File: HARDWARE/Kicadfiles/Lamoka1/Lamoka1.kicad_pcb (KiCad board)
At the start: 2 copper layers, 156.4 x 124.8 mm, 139 parts, among them IC1 INA240A2DR, J1 2606-1108/010-000, J2 2606-1352, J3 USB_C_Receptacle_USB2.0_14P, J4 470531000, J5 2604-1103, J6 Male-Header, J7 Male-Header, Q1 25V 60A N-Ch, Q2 30V 56A N-Ch, Q3 100V 150A N-Ch, Q4 100V 150A N-Ch, Q5 100V 150A N-Ch, Q6 100V 150A N-Ch, SW1 B3F-4055, U1 RP2354A, U10 ADS7128IRTER, U2 AMS1117-3.3, U3 74AHCT1G125, U4 LM5122MH/NOPB, U5 UCC27735DR, U6 UCC27735DR, U7 TPS62160DSGR, U8 TMP235A2DBZR, U9 TMP235A2DBZR, X1 ABM8-272-T3

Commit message: misc fixes
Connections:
- net /Battery-Connection  renamed +BATT
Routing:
- net GND: track 29.3 -> 31.6 mm
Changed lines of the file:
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@@
 		(sheetname "/Inversion-Section/")
 		(sheetfile "Inversion-section.kicad_sch")
+		(units
+			(unit
+				(name "A")
+				(pins "2" "1" "3")
+			)
+		)
 		(attr smd)
 		(duplicate_pad_numbers_are_jumpers no)
@@
 		(sheetname "/")
 		(sheetfile "Lamoka1.kicad_sch")
+		(units
+			(unit
+				(name "A")
+				(pins "1" "2" "3" "4" "5" "6")
+			)
+		)
 		(attr through_hole)
 		(duplicate_pad_numbers_are_jumpers no)
@@
 			(layers "F.Cu" "F.Mask" "F.Paste")
 			(roundrect_rratio 0.204082)
-			(net "/Battery-Connection ")
+			(net "+BATT")
 			(pintype "passive")
 		)
@@
 			(net "unconnected-(U10-AIN5{slash}GPIO5-Pad4)")
 			(pinfunction "AIN5/GPIO5_4")
-			(pintype "bidirectional")
+			(pintype "bidirectional+no_connect")
 		)
 		(pad "5" smd rect
@@
 			(net "unconnected-(U10-AIN6{slash}GPIO6-Pad5)")
 			(pinfunction "AIN6/GPIO6_5")
-			(pintype "bidirectional")
+			(pintype "bidirectional+no_connect")
 		)
 		(pad "6" smd rect
@@
 			(net "unconnected-(U10-AIN7{slash}GPIO7-Pad6)")
 			(pinfunction "AIN7/GPIO7_6")
-			(pintype "bidirectional")
+			(pintype "bidirectional+no_connect")
 		)
 		(pad "7" smd rect
@@
 			(net "GND")
 			(pinfunction "GND_9")
-			(pintype "power_out")
+			(pintype "power_in")
 		)
 		(pad "10" smd rect
@@
 			(net "GND")
 			(pinfunction "GND_17")
-			(pintype "power_out")
+			(pintype "power_in")
 		)
 		(embedded_fonts no)
@@
 			(net "/Control-Section/PG")
 			(pinfunction "PG_8")
-			(pintype "input")
+			(pintype "open_collector")
 		)
 		(pad "9" smd rect
@@
 			(net "GND")
 			(pinfunction "VSS_3")
-			(pintype "power_out")
+			(pintype "power_in")
 		)
 		(pad "4" smd rect
@@
 			(net "GND")
 			(pinfunction "COM_5")
-			(pintype "output")
+			(pintype "passive")
 		)
 		(pad "6" smd rect
@@
 		(sheetname "/Inversion-Section/")
 		(sheetfile "Inversion-section.kicad_sch")
+		(units
+			(unit
+				(name "A")
+				(pins "2" "1" "3")
+			)
+		)
 		(attr smd)
 		(duplicate_pad_numbers_are_jumpers no)
@@
 			(net "unconnected-(U4-SYNCOUT-Pad1)")
 			(pinfunction "SYNCOUT_1")
-			(pintype "output")
+			(pintype "output+no_connect")
 		)
 		(pad "2" smd rect
@@
 		(sheetname "/Control-Section/")
 		(sheetfile "Control-section.kicad_sch")
+		(units
+			(unit
+				(name "A")
+				(pins "1" "2")
+			)
+		)
 		(attr smd)
 		(duplicate_pad_numbers_are_jumpers no)
@@
 			(net "GND")
 			(pinfunction "VSS_3")
-			(pintype "power_out")
+			(pintype "power_in")
 		)
 		(pad "4" smd rect
@@
 			(net "GND")
 			(pinfunction "COM_5")
-			(pintype "output")
+			(pintype "passive")
 		)
 		(pad "6" smd rect
@@
 		(sheetname "/")
 		(sheetfile "Lamoka1.kicad_sch")
+		(units
+			(unit
+				(name "A")
+				(pins "1" "2" "3" "4" "5" "6" "7" "8")
+			)
+		)
 		(attr through_hole)
 		(duplicate_pad_numbers_are_jumpers no)
@@
 			(size 0.65 1.528)
 			(layers "F.Cu" "F.Mask" "F.Paste")
-			(net "/Battery-Connection ")
+			(net "+BATT")
 			(pinfunction "IN+_8")
 			(pintype "passive")
@@
 		(sheetname "/Control-Section/")
 		(sheetfile "Control-section.kicad_sch")
+		(units
+			(unit
+				(name "A")
+				(pins "1" "2")
+			)
+		)
 		(attr smd)
 		(duplicate_pad_numbers_are_jumpers no)
@@
 		(sheetname "/Control-Section/")
 		(sheetfile "Control-section.kicad_sch")
+		(units
+			(unit
+				(name "A")
+				(pins "1" "2")
+			)
+		)
 		(attr smd)
 		(duplicate_pad_numbers_are_jumpers no)
@@
 			(layers "*.Cu" "*.Mask")
 			(remove_unused_layers no)
-			(net "/Battery-Connection ")
+			(net "+BATT")
 			(pinfunction "1_1_1")
 			(pintype "unspecified")
@@
 			(layers "*.Cu" "*.Mask")
 			(remove_unused_layers no)
-			(net "/Battery-Connection ")
+			(net "+BATT")
 			(pinfunction "1_2_2")
 			(pintype "unspecified")
@@
 			(net "/Control-Section/3v3")
 			(pinfunction "VOUT_2")
-			(pintype "output")
+			(pintype "power_out")
 		)
 		(pad "2" smd roundrect
@@
 			(net "/Control-Section/3v3")
 			(pinfunction "VOUT_2")
-			(pintype "output")
+			(pintype "power_out")
 		)
 		(pad "3" smd roundrect
@@
 	)
 	(segment
+		(start 140.185558 117.576297)
+		(end 139.86056 117.251299)
+		(width 0.4)
+		(layer "F.Cu")
+		(net "GND")
+	)
+	(segment
 		(start 111.518109 95.568109)
 		(end 111.518109 95.524454)
@@
 	)
 	(segment
+		(start 140.185558 119.426301)
+		(end 140.185558 117.576297)
+		(width 0.4)
+		(layer "F.Cu")
+		(net "GND")
+	)
+	(segment
 		(start 109.663201 102.2068)
 		(end 109.663201 102.929999)
@@
 	)
 	(via
-		(at 88.55 134.77)
+		(at 88.77 135.4)
 		(size 0.6)
 		(drill 0.3)
@@
 	)
 	(via
-		(at 140.185558 118.775)
+		(at 137.67 114.46)
 		(size 0.6)
 		(drill 0.3)
@@
 	)
 	(via
-		(at 88.48 136.04)
+		(at 88.79 138.1)
 		(size 0.6)
 		(drill 0.3)
@@
 	)
 	(segment
-		(start 102.761 133.2835)
-		(end 99.7575 130.28)
-		(width 0.55)
-		(layer "F.Cu")
-		(net "/Battery-Connection ")
-	)
-	(segment
-		(start 65.2 129.97)
-		(end 65.2 142.47)
-		(width 2.25)
-		(layer "F.Cu")
-		(net "/Battery-Connection ")
-	)
-	(segment
-		(start 102.761 135.485)
-		(end 102.761 133.2835)
-		(width 0.55)
-		(layer "F.Cu")
-		(net "/Battery-Connection ")
-	)
-	(segment
 		(start 113.38 115.05)
 		(end 110.300733 118.129267)
@@
 		(net "/Inversion-Section/HB1")
 	)
+	(segment
+		(start 102.761 133.2835)
+		(end 99.7575 130.28)
+		(width 0.55)
+		(layer "F.Cu")
+		(net "+BATT")
+	)
+	(segment
+		(start 65.2 129.97)
+		(end 65.2 142.47)
+		(width 2.25)
+		(layer "F.Cu")
+		(net "+BATT")
+	)
+	(segment
+		(start 102.761 135.485)
+		(end 102.761 133.2835)
+		(width 0.55)
+		(layer "F.Cu")
+		(net "+BATT")
+	)
 	(zone
 		(net "/BROWN")
@@
 	)
 	(zone
-		(net "/Battery-Connection ")
-		(layer "F.Cu")
-		(name "Battery-connection")
-		(hatch edge 0.5)
-		(priority 46)
-		(connect_pads yes
-			(clearance 0.25)
-		)
-		(min_thickness 0.1)
-		(fill yes
-			(thermal_gap 0.5)
-			(thermal_bridge_width 0.5)
-			(smoothing fillet)
-			(radius 0.55)
-			(island_removal_mode 0)
-		)
-		(polygon
-			(pts
-				(xy 100.41 128.54) (xy 100.44 131.93) (xy 95.44 131.8) (xy 91.73 132.31) (xy 90.64 132.8) (xy 89.22 133.15)
-				(xy 88.24 133.66) (xy 87.27 134.55) (xy 86.84 136.11) (xy 85.93 137.07) (xy 83.86 138.29) (xy 81.76 138.97)
-				(xy 80.37 139.35) (xy 78.62 139.27) (xy 76.05 139.68) (xy 71.44 141.15) (xy 69.5 141.98) (xy 68.1 142.94)
-				(xy 65.93 144.56) (xy 63.48 145.04) (xy 62.84 144.31) (xy 62.41 141.9) (xy 62.29 140.01) (xy 62.57 137.2)
-				(xy 62.44 134.9) (xy 62.36 132.93) (xy 62.77 131.49) (xy 62.97 130.28) (xy 63.12 128.63) (xy 64.01 128.1)
-				(xy 64.61 127.97) (xy 65.98 128.02) (xy 67.12 128.45) (xy 67.7 129.41) (xy 68.13 130.28) (xy 74.22 131.41)
-				(xy 75.36 132.67) (xy 76.98 133.36) (xy 79.33 132.95) (xy 80.83 132.32) (xy 82.52 130.28) (xy 83.78 128.75)
-			)
-		)
-	)
-	(zone
 		(net "Net-(U1-VREG_AVDD)")
 		(layer "F.Cu")
@@
 	)
 	(zone
+		(net "+BATT")
+		(layer "F.Cu")
+		(name "batt")
+		(hatch edge 0.5)
+		(priority 46)
+		(connect_pads yes
+			(clearance 0.5)
+		)
+		(min_thickness 0.25)
+		(fill yes
+			(thermal_gap 0.5)
+			(thermal_bridge_width 0.5)
+			(smoothing fillet)
+			(radius 0.5)
+			(island_removal_mode 0)
+		)
+		(polygon
+			(pts
+				(xy 63.38121 128.16751) (xy 63.238811 144.35) (xy 67.51 144.39) (xy 71.81 139.44) (xy 73.51 137.49)
+				(xy 93.679075 132.103717) (xy 100.534871 132.156699) (xy 100.56 128.460928) (xy 98.55631 128.449265)
+				(xy 94 128.51) (xy 73.13 133.21) (xy 66.755645 128.086308)
+			)
+		)
+	)
+	(zone
 		(net "/Inversion-Section/Q4G")
 		(layer "F.Cu")
@@
 		(name "GND")
 		(hatch edge 0.5)
-		(connect_pads
+		(connect_pads yes
 			(clearance 0.5)
 		)

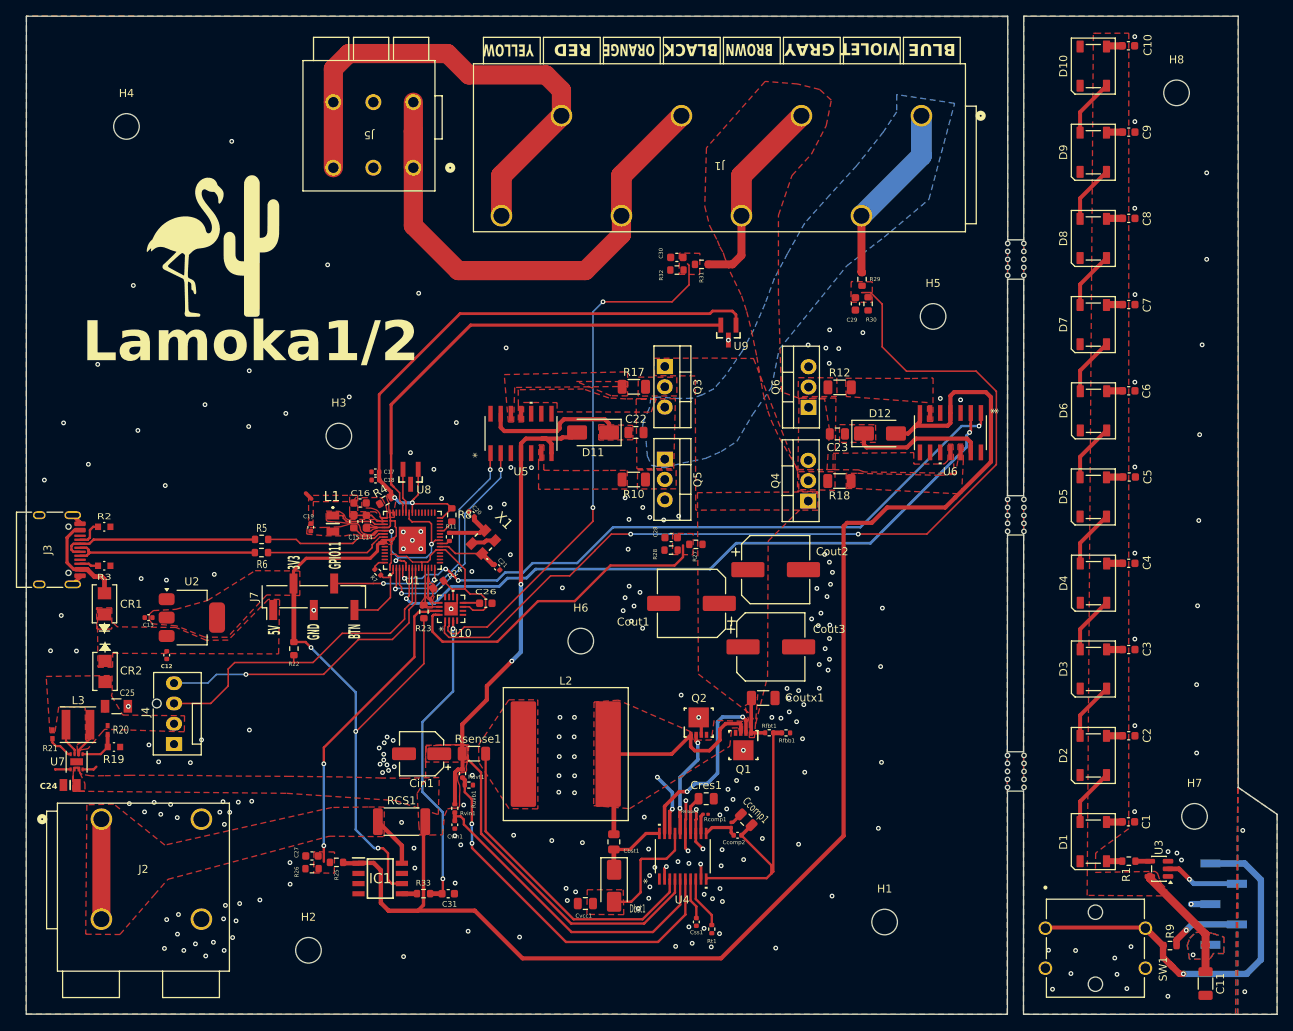
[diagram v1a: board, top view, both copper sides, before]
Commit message: General fixes, laying H bridge transformers side by side for more effective heat dissapation. fixed footprints to datasheet specific
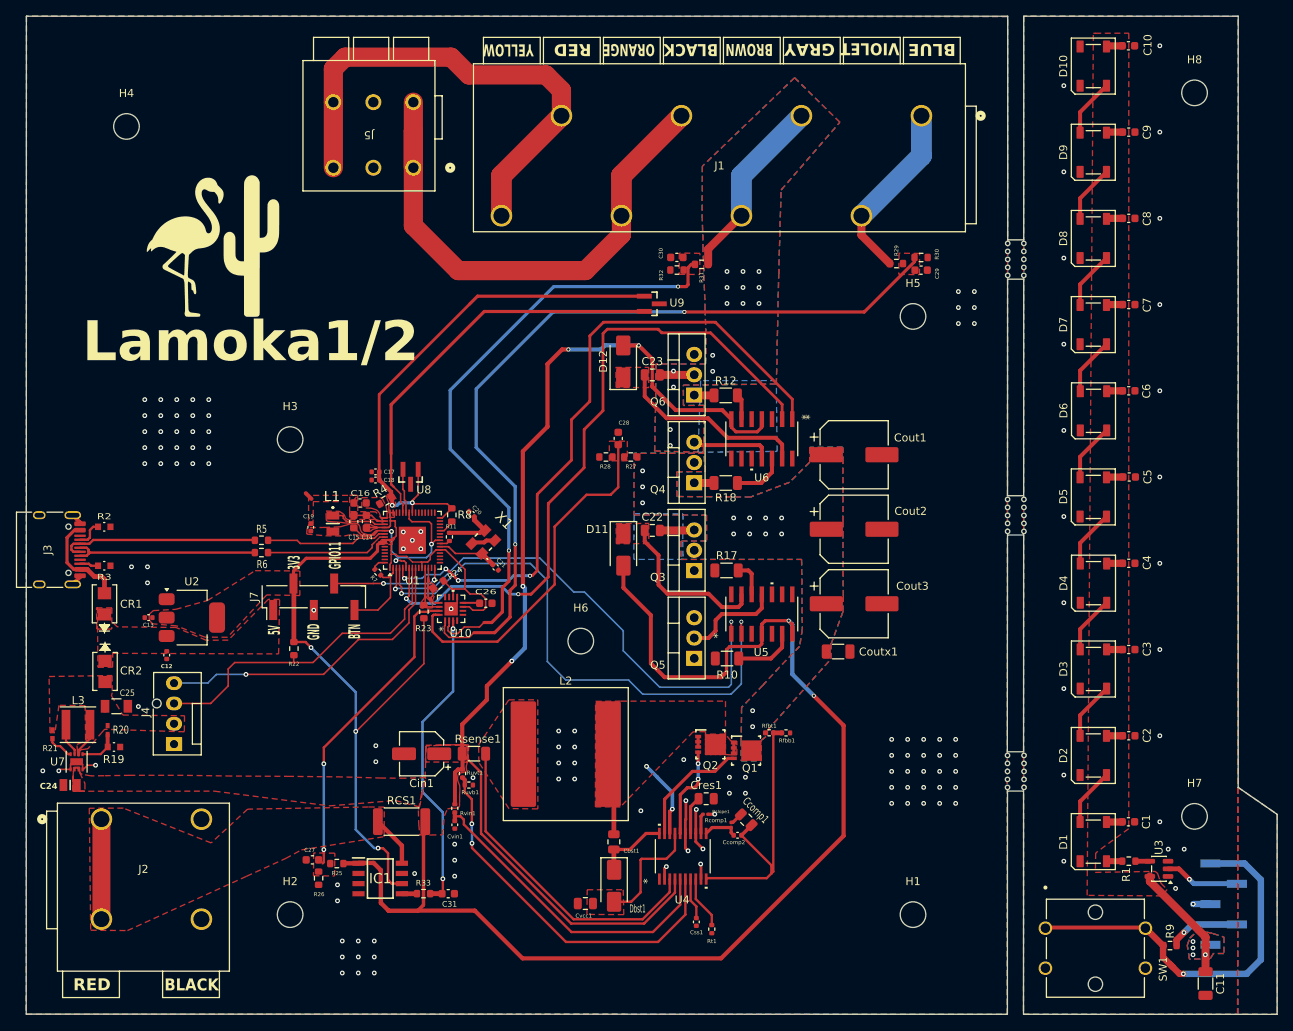
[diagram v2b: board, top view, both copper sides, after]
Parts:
- moved U5 37.6 mm to (147.8, 104.3)
- moved D12 33.3 mm to (130.4, 72.8), turned to 90 degrees
- moved Cout1 27.5 mm to (159.3, 84.4), turned to 0 degrees
- moved Q3 25.8 mm to (139.3, 98.9), turned to 90 degrees
- moved R17 25.7 mm to (143.3, 98.9), turned to 180 degrees
- moved R10 25.2 mm to (143.4, 109.9), turned to 0 degrees
- moved Q5 25.2 mm to (139.3, 109.9), turned to 90 degrees
- moved C23 24.3 mm to (134.1, 74.4), turned to 0 degrees
- moved U6 23.6 mm to (147.8, 82.4)
- moved D11 15.1 mm to (130.4, 96.3), turned to -90 degrees
- moved Q4 14.4 mm to (139.3, 87.9)
- moved Q6 14.4 mm to (139.3, 77.0)
- moved R12 14.3 mm to (143.2, 77.0)
- moved R18 14.2 mm to (143.2, 88.0)
- moved R28 14.2 mm to (128.3, 84.7)
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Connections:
- Q1 pad 1: /Inversion-Section/G4D -> /Inversion-Section/SW
- Q1 pad 2: /Inversion-Section/HO -> /Inversion-Section/SW
- Q1 pad 4: (no net) -> /Inversion-Section/HO
- Q1 pad 9: GND -> /Inversion-Section/G4D
- Q2 pad 1: /Inversion-Section/SW -> GND
- Q2 pad 2: /Inversion-Section/LO -> GND
- Q2 pad 4: (no net) -> /Inversion-Section/LO
- Q2 pad 9: GND -> /Inversion-Section/SW
- Q3 pad 1: /Inversion-Section/G4D -> /Inversion-Section/Q3G
- Q3 pad 2: /Inversion-Section/Q3G -> /Inversion-Section/G4D
- Q4 pad 1: /Inversion-Section/G4D -> /Inversion-Section/Q4G
- Q4 pad 2: /Inversion-Section/Q4G -> /Inversion-Section/G4D
- Q5 pad 1: /BLUE -> /Inversion-Section/Q5G
- Q5 pad 2: /Inversion-Section/Q5G -> /BLUE
- Q6 pad 1: /BROWN -> /Inversion-Section/Q6G
- Q6 pad 2: /Inversion-Section/Q6G -> /BROWN
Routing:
- net /Control-Section/GPIO2: track 28.4 -> 70.0 mm
- net /Control-Section/GPIO1: track 27.4 -> 64.1 mm
- net /Inversion-Section/CSP: track 277.5 -> 299.3 mm, vias 2 -> 6
- net /Inversion-Section/SW: track 40.8 -> 21.5 mm
- net /BLUE: track 22.7 -> 39.9 mm
- net /BROWN: track 25.2 -> 37.8 mm, vias 0 -> 15
- net /Control-Section/3v3: track 197.6 -> 186.2 mm
- net /Control-Section/AIN3: track 67.7 -> 78.8 mm
- net /Control-Section/AIN2: track 114.0 -> 103.8 mm
- net /Control-Section/TEMP_INV: track 59.4 -> 50.6 mm
- net /Inversion-Section/HO: track 23.7 -> 15.0 mm, vias 2 -> 0
- net /Inversion-Section/LO1: track 0.00 -> 7.70 mm
- net /Inversion-Section/HB2: track 16.8 -> 24.1 mm
- net Net-(U6-HO): track 0.00 -> 6.59 mm
- net /Inversion-Section/G4D: track 6.11 -> 0.00 mm, vias 0 -> 11
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- added copper zone on B.Cu, net /BROWN
- added copper zone on B.Cu, net /Inversion-Section/G4D
- removed copper zone on B.Cu, net /BLUE
- removed copper zone on F.Cu, net /BLUE
- removed copper zone on F.Cu, net /Inversion-Section/LO1
- removed copper zone on F.Cu, net /Inversion-Section/LO2
- removed copper zone on F.Cu, net /Inversion-Section/Q3G
- removed copper zone on F.Cu, net /Inversion-Section/Q4G
- removed copper zone on F.Cu, net /Inversion-Section/Q5G
- removed copper zone on F.Cu, net /Inversion-Section/Q6G
- removed copper zone on F.Cu, net Net-(U5-HO)
- removed copper zone on F.Cu, net Net-(U6-HO)

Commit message: major reform on the size of the Lamoka1/2
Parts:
- removed C10, C6, C7, C8, C9: 100n, Capacitor_SMD:C_0603_1608Metric
- removed D10, D7, D8, D9: WS2812B, LED_SMD:LED_WS2812B_PLCC4_5.0x5.0mm_P3.2mm
- removed the D6 at (189.2, 78.9)
- removed J6, J7: Male-Header, Connector_PinHeader_2.54mm:PinHeader_1x05_P2.54mm_Vertical_SMD_Pin1Left
- removed MTB1, MTB2, MTB3: MouseBite-5x0.55, MouseBite-5x0.55
- C12, C13, C20, C21, C24, C25, CR1, CR2, D11, D12, J3, L1, R11, R19, R2, R20, R21, R3, R5, R6, R8, U1, U10, U2, U5, U6, U7, X1: moved to B.Cu
- L3: value 2.2uH, 4.3A -> 2.2uH; moved to B.Cu
- moved G*** 455.0 mm to (517.3, 181.2)
- moved C13 387.0 mm to (395.9, 315.3)
- moved U2 387.0 mm to (401.3, 315.3)
- moved C12 382.0 mm to (398.1, 310.6), turned to -90 degrees
- moved CR1 378.0 mm to (380.4, 312.3)
- moved CR2 341.3 mm to (349.7, 300.7)
- moved L3 334.8 mm to (349.9, 289.4), turned to -90 degrees
- moved R21 332.9 mm to (346.2, 287.8), turned to 180 degrees
- moved U7 330.0 mm to (344.9, 292.8), turned to 0 degrees
- moved R20 327.9 mm to (346.2, 289.1), turned to 180 degrees
- moved D12 327.7 mm to (421.0, 224.2)
- moved C24 327.6 mm to (342.5, 293.8), turned to -90 degrees
- moved C25 327.4 mm to (347.0, 285.8), turned to 0 degrees
- moved D11 327.3 mm to (421.1, 246.8)
- moved R19 323.8 mm to (343.4, 289.1), turned to 180 degrees
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- renumbered Cbst1 to C32, Cvcc1 to C33, Dbst1 to D6
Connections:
- C1 pad 1: /User-Interface-Section/5V -> /Control-Section/5V
- C11 pad 1: /User-Interface-Section/5V -> /Control-Section/5V
- C2 pad 1: /User-Interface-Section/5V -> /Control-Section/5V
- C3 pad 1: /User-Interface-Section/5V -> /Control-Section/5V
- C4 pad 1: /User-Interface-Section/5V -> /Control-Section/5V
- C5 pad 1: /User-Interface-Section/5V -> /Control-Section/5V
- D1 pad 1: /User-Interface-Section/5V -> /Control-Section/5V
- D2 pad 1: /User-Interface-Section/5V -> /Control-Section/5V
- D3 pad 1: /User-Interface-Section/5V -> /Control-Section/5V
- D4 pad 1: /User-Interface-Section/5V -> /Control-Section/5V
- D5 pad 1: /User-Interface-Section/5V -> /Control-Section/5V
- D5 pad 2: Net-(D5-DOUT) -> unconnected-(D5-DOUT-Pad2)
- R9 pad 1: /User-Interface-Section/3v3 -> /Control-Section/3v3
- R9 pad 2: /User-Interface-Section/BTN -> /Control-Section/BTN
- SW1 pad 1: /User-Interface-Section/BTN -> /Control-Section/BTN
- SW1 pad 2: /User-Interface-Section/BTN -> /Control-Section/BTN
- U3 pad 2: /User-Interface-Section/GPIO11 -> /Control-Section/GPIO11
- U3 pad 5: /User-Interface-Section/5V -> /Control-Section/5V
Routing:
- net /Inversion-Section/G4D: track 0.00 -> 238.8 mm, vias 11 -> 0
- net /Inversion-Section/CSP: track 299.3 -> 82.5 mm, vias 6 -> 0
- net /Control-Section/3v3: track 186.2 -> 0.00 mm, vias 5 -> 0
- net /Control-Section/AIN2: track 103.8 -> 0.53 mm, vias 2 -> 0
- net /Control-Section/GPIO4: track 85.7 -> 0.00 mm, vias 2 -> 0
- net /Control-Section/GPIO3: track 84.2 -> 0.00 mm, vias 4 -> 0
- net /Control-Section/AIN3: track 78.8 -> 0.45 mm, vias 2 -> 0
- net /Control-Section/GPIO2: track 70.0 -> 0.00 mm, vias 2 -> 0
- net /Control-Section/GPIO1: track 64.1 -> 0.00 mm, vias 2 -> 0
- net /Control-Section/TEMP_INV: track 50.6 -> 0.00 mm
- net /User-Interface-Section/BTN: track 48.7 -> 0.00 mm, vias 1 -> 0
- net /Inversion-Section/UVLO: track 46.7 -> 1.00 mm, vias 2 -> 0
- net /Control-Section/AIN1: track 44.2 -> 0.00 mm
- net /GPIO5: track 42.2 -> 0.03 mm
- net /Inversion-Section/CSN: track 40.3 -> 0.00 mm
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- removed copper zone on F.Cu, net +BATT
- removed copper zone on B.Cu, net /BROWN
- removed copper zone on F.Cu, net /BROWN
- removed copper zone on F.Cu, net /Buck-5v
- removed copper zone on F.Cu, net /Control-Section/1V1
- removed copper zone on F.Cu, net /Control-Section/3v3
- removed copper zone on F.Cu, net /Control-Section/5V
- removed copper zone on F.Cu, net /Control-Section/AIN0
- removed copper zone on F.Cu, net /Control-Section/AIN1
- removed copper zone on F.Cu, net /Control-Section/GPIO8
- removed copper zone on F.Cu, net /Control-Section/GPIO9
- removed copper zone on F.Cu, net /Control-Section/VREG_GND
- removed copper zone on F.Cu, net /Inversion-Section/CSN
- removed copper zone on F.Cu, net /Inversion-Section/CSP
- removed copper zone on B.Cu, net /Inversion-Section/G4D
- removed copper zone on F.Cu, net /Inversion-Section/G4D
- removed copper zone on F.Cu, net /Inversion-Section/HB1
- removed copper zone on F.Cu, net /Inversion-Section/HB2
- removed copper zone on F.Cu, net /Inversion-Section/SW
- removed copper zone on F.Cu, net /Inversion-Section/VCC
- removed copper zone on B.Cu, net /User-Interface-Section/5V
- removed copper zone on F.Cu, net /User-Interface-Section/5V
- removed copper zone on B.Cu, net GND
- removed copper zone on F.Cu, net GND
- removed copper zone on F.Cu, net Net-(U1-VREG_AVDD)
- removed copper zone on F.Cu, net Net-(U1-VREG_LX)
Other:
- board size 156.4 x 124.8 mm -> 95 x 95 mm
- board text added: "Danger! High Voltage"
- board text removed: "3V3"
- board text removed: "5V"
- board text removed: "BTN"
- board text removed: "Danger! High Voltage."
- board text removed: "GND"
- board text removed: "GPIO11"

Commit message: misc fixes to the Lamoka1/2, more routing and all that fun stuff
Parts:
- moved H2 167.6 mm to (231.3, 128.7)
- moved R33 157.2 mm to (359.9, 249.6)
- moved C31 149.8 mm to (363.0, 249.6)
- moved H1 123.1 mm to (260.3, 164.2)
- moved H6 113.4 mm to (275.8, 152.4)
- moved H4 110.8 mm to (252.8, 118.8)
- moved H3 104.9 mm to (251.7, 145.1)
- moved CR1 94.6 mm to (342.2, 225.8)
- moved H5 85.6 mm to (275.6, 127.4)
- moved C12 84.2 mm to (361.1, 235.0)
- moved C13 84.2 mm to (358.9, 239.6)
- moved U2 84.2 mm to (364.3, 239.6)
- moved CR2 62.3 mm to (349.9, 238.4), turned to 180 degrees
- moved C25 46.8 mm to (344.9, 239.0)
- moved C24 46.8 mm to (340.4, 247.1)
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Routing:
- net /Inversion-Section/CSP: track 82.5 -> 157.9 mm
- net /Buck-5v: track 11.8 -> 49.9 mm
- net /Control-Section/AIN2: track 0.53 -> 21.6 mm
- net /Control-Section/AIN3: track 0.45 -> 19.3 mm
- net Net-(IC1-OUT): track 0.00 -> 17.7 mm
- net /Control-Section/AIN4: track 0.00 -> 12.0 mm
- removed copper zone on F.Cu, net /Control-Section/AIN2
- removed copper zone on F.Cu, net /Control-Section/AIN3
